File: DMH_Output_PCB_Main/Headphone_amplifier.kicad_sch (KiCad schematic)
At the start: 26 parts, among them J12 Conn_01x06_PinHeader, J27 Conn_01x06_PinHeader, U11 TL074, U12 NE5532, U13 NE5532, U14 NE5532, U15 NE5532

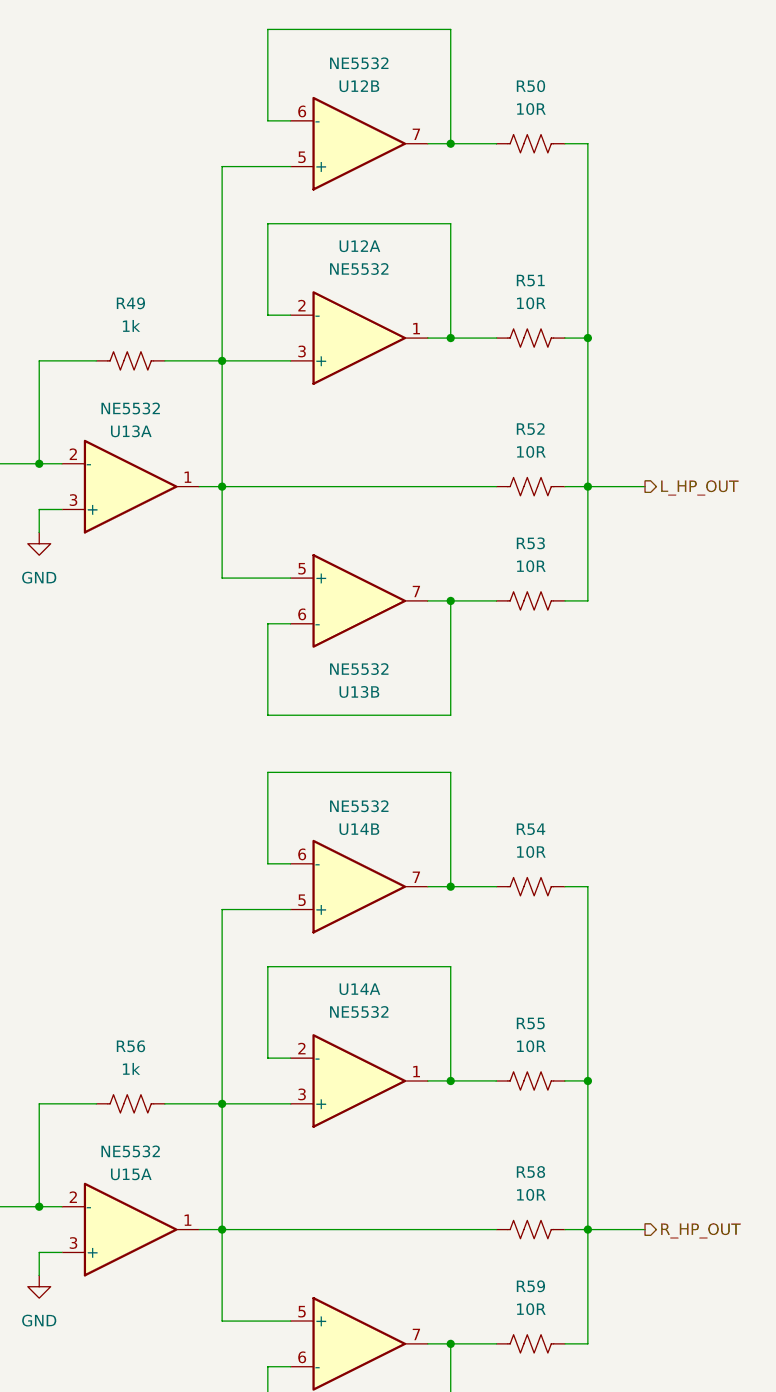
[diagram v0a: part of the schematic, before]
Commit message: Removed 2 extra OpAmps from the headphone amp
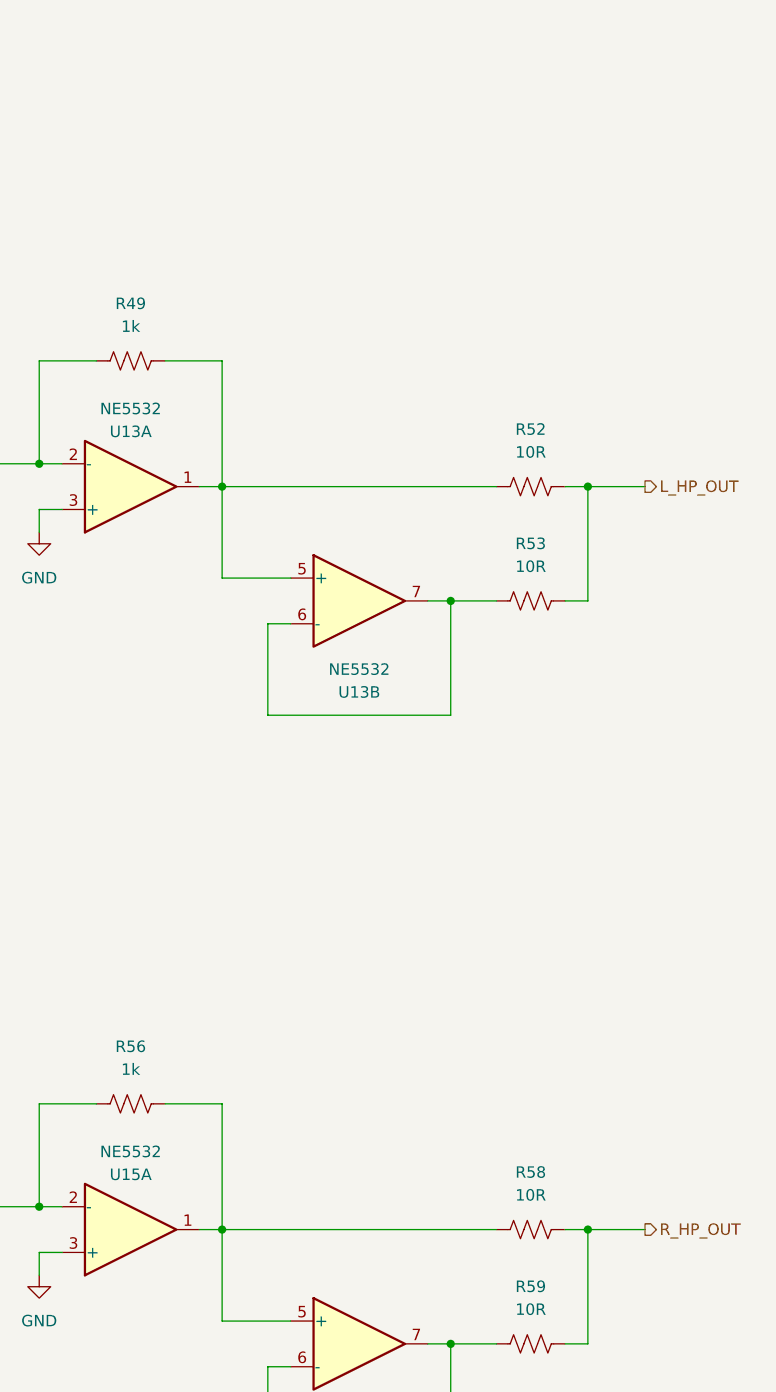
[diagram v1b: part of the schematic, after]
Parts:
- removed R50, R51, R54, R55: 10R, Resistor_THT:R_Axial_DIN0207_L6.3mm_D2.5mm_P7.62mm_Horizontal, symbol Device:R_US
- removed U12, U14: NE5532, Package_DIP:DIP-8_W7.62mm_Socket, symbol Amplifier_Operational:NE5532

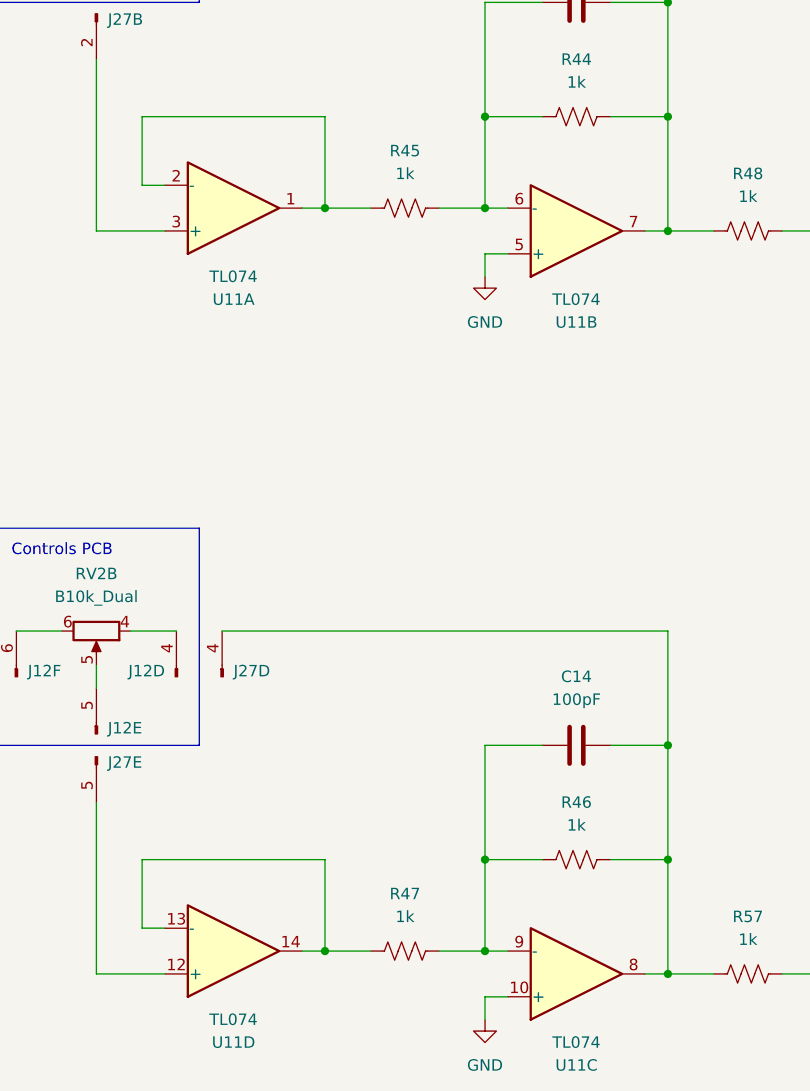
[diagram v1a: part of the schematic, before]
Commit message: Changed headphone amp max gain
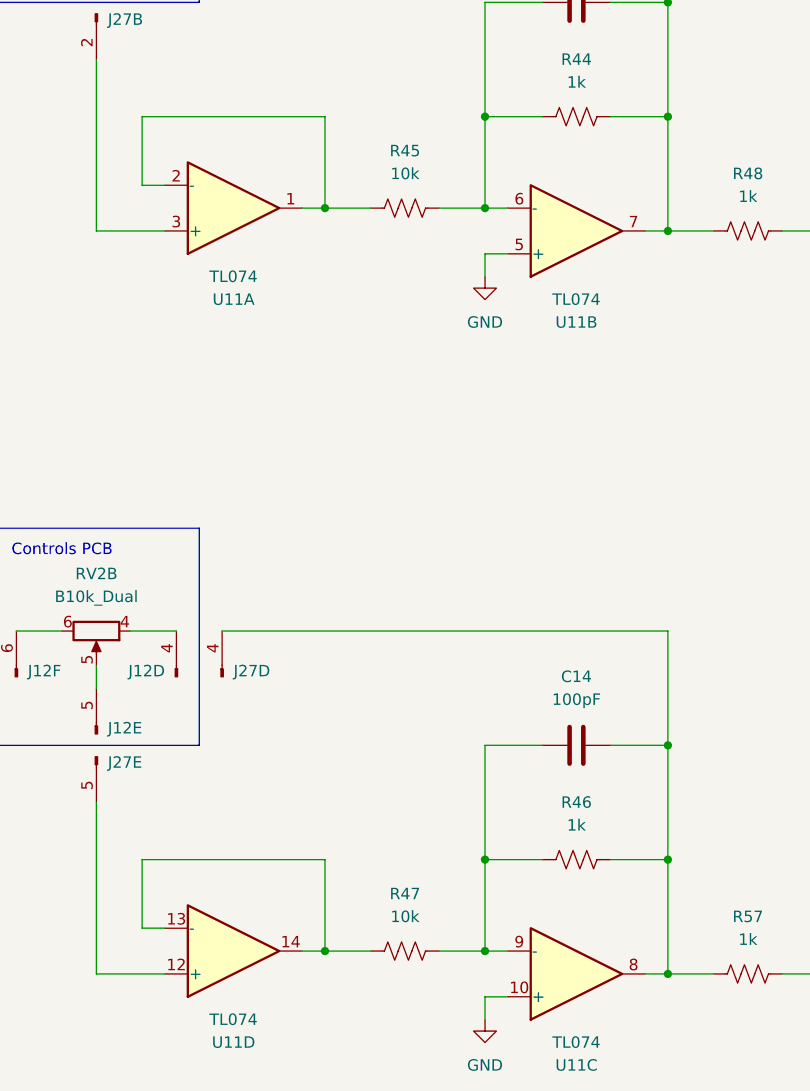
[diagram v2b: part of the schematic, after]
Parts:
- R45, R47: value 1k -> 10k
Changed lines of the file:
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@@
 			)
 		)
-		(property "Value" "1k"
+		(property "Value" "10k"
 			(at 76.2 57.15 90)
 			(show_name no)
@@
 			)
 		)
-		(property "Value" "1k"
+		(property "Value" "10k"
 			(at 76.2 139.7 90)
 			(show_name no)

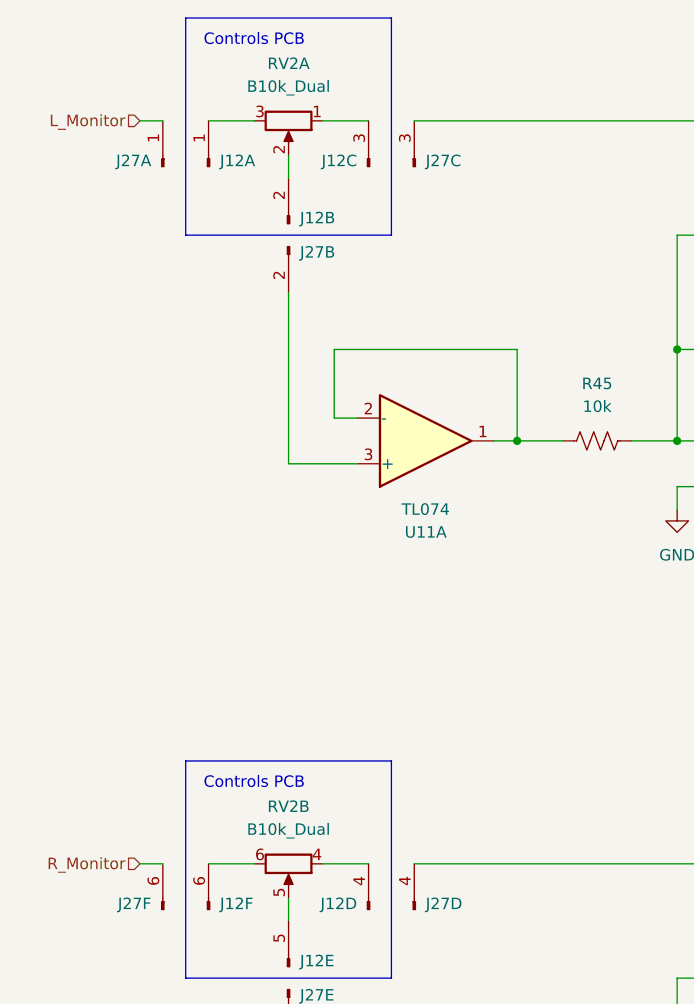
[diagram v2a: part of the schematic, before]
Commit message: Replaced jack symbols with 5pin ones
Also updated Meter LED current source resistor to 75R
Also increased LED guiding PCB mounting holes to M2.5
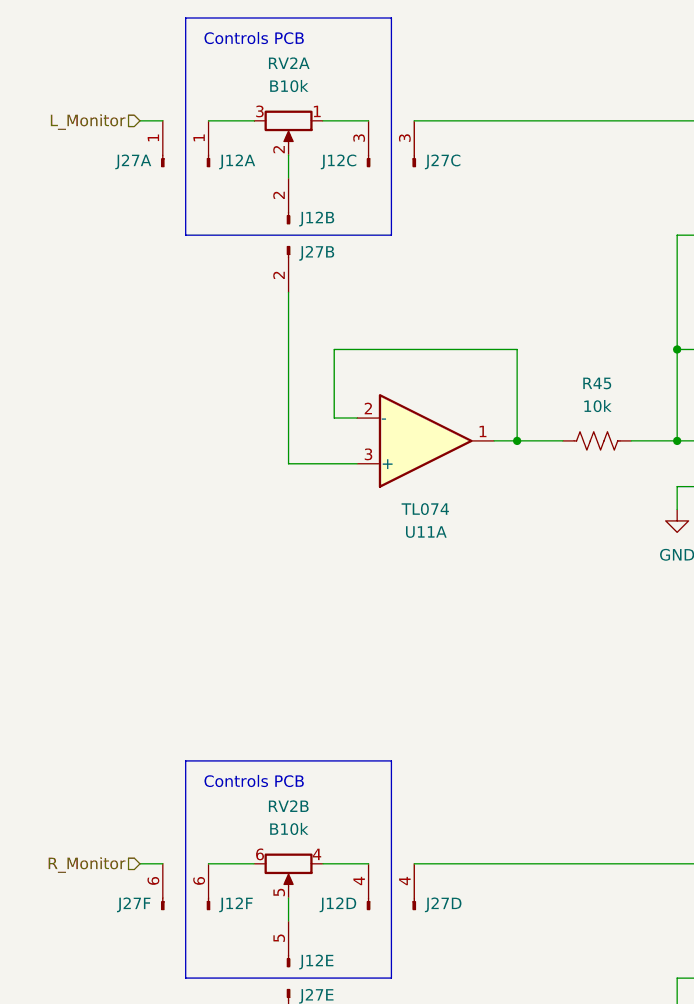
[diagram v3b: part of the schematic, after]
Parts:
- RV2: value B10k_Dual -> B10k; footprint Potentiometer_THT:Potentiometer_Alpha_RD902F-40-00D_Dual_Vertical -> SynthStuff:Potentiometer_Alpha_RD902F-40-00D_Dual_Vertical
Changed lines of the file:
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@@
 			)
 		)
-		(property "Value" "B10k_Dual"
+		(property "Value" "B10k"
 			(at 41.91 104.14 90)
 			(show_name no)
@@
 			)
 		)
-		(property "Footprint" "Potentiometer_THT:Potentiometer_Alpha_RD902F-40-00D_Dual_Vertical"
+		(property "Footprint" "SynthStuff:Potentiometer_Alpha_RD902F-40-00D_Dual_Vertical"
 			(at 41.91 107.95 0)
 			(hide yes)
@@
 					(bold yes)
 					(italic yes)
+				)
+			)
+		)
+		(property "Sim.Library" "${KICAD9_SYMBOL_DIR}/Simulation_SPICE.sp"
+			(at 41.91 107.95 0)
+			(hide yes)
+			(show_name no)
+			(do_not_autoplace no)
+			(effects
+				(font
+					(size 1.27 1.27)
+				)
+			)
+		)
+		(property "Sim.Name" "pot_dual"
+			(at 41.91 107.95 0)
+			(hide yes)
+			(show_name no)
+			(do_not_autoplace no)
+			(effects
+				(font
+					(size 1.27 1.27)
+				)
+			)
+		)
+		(property "Sim.Device" "SUBCKT"
+			(at 41.91 107.95 0)
+			(hide yes)
+			(show_name no)
+			(do_not_autoplace no)
+			(effects
+				(font
+					(size 1.27 1.27)
+				)
+			)
+		)
+		(property "Sim.Pins" "1=r1A 2=wA 3=r0A 4=r1B 5=wB 6=r0B"
+			(at 41.91 107.95 0)
+			(hide yes)
+			(show_name no)
+			(do_not_autoplace no)
+			(effects
+				(font
+					(size 1.27 1.27)
+				)
+			)
+		)
+		(property "Sim.Params" "Rtot=1 wpos=0.4"
+			(at 41.91 107.95 0)
+			(hide yes)
+			(show_name no)
+			(do_not_autoplace no)
+			(effects
+				(font
+					(size 1.27 1.27)
 				)
 			)
@@
 			)
 		)
-		(property "Value" "B10k_Dual"
+		(property "Value" "B10k"
 			(at 41.91 21.59 90)
 			(show_name no)
@@
 			)
 		)
-		(property "Footprint" "Potentiometer_THT:Potentiometer_Alpha_RD902F-40-00D_Dual_Vertical"
+		(property "Footprint" "SynthStuff:Potentiometer_Alpha_RD902F-40-00D_Dual_Vertical"
 			(at 41.91 25.4 0)
 			(hide yes)
@@
 				)
 			)
+		)
+		(property "Sim.Library" "${KICAD9_SYMBOL_DIR}/Simulation_SPICE.sp"
+			(at 41.91 25.4 0)
+			(hide yes)
+			(show_name no)
+			(do_not_autoplace no)
+			(effects
+				(font
+					(size 1.27 1.27)
+				)
+			)
+		)
+		(property "Sim.Name" "pot_dual"
+			(at 41.91 25.4 0)
+			(hide yes)
+			(show_name no)
+			(do_not_autoplace no)
+			(effects
+				(font
+					(size 1.27 1.27)
+				)
+			)
+		)
+		(property "Sim.Device" "SUBCKT"
+			(at 41.91 25.4 0)
+			(hide yes)
+			(show_name no)
+			(do_not_autoplace no)
+			(effects
+				(font
+					(size 1.27 1.27)
+				)
+			)
+		)
+		(property "Sim.Pins" "1=r1A 2=wA 3=r0A 4=r1B 5=wB 6=r0B"
+			(at 41.91 25.4 0)
+			(hide yes)
+			(show_name no)
+			(do_not_autoplace no)
+			(effects
+				(font
+					(size 1.27 1.27)
+				)
+			)
+		)
+		(property "Sim.Params" "Rtot=1 wpos=0.4"
+			(at 41.91 25.4 0)
+			(hide yes)
+			(show_name no)
+			(do_not_autoplace no)
+			(effects
+				(font
+					(size 1.27 1.27)
+				)
+			)

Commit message: Prepped for Main PCB design
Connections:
- net L_HP_OUT renamed L_HP_OUT_M
- net L_Monitor renamed L_HP_IN_M
- net R_HP_OUT renamed R_HP_OUT_M
- net R_Monitor renamed R_HP_IN_M
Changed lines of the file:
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@@
 		)
 	)
-	(hierarchical_label "R_HP_OUT"
+	(hierarchical_label "R_HP_OUT_M"
 		(shape output)
 		(at 190.5 148.59 0)
@@
 		)
 	)
-	(hierarchical_label "R_Monitor"
+	(hierarchical_label "R_HP_IN_M"
 		(shape input)
 		(at 25.4 107.95 180)
@@
 		)
 	)
-	(hierarchical_label "L_Monitor"
+	(hierarchical_label "L_HP_IN_M"
 		(shape input)
 		(at 25.4 25.4 180)
@@
 		)
 	)
-	(hierarchical_label "L_HP_OUT"
+	(hierarchical_label "L_HP_OUT_M"
 		(shape output)
 		(at 190.5 66.04 0)
